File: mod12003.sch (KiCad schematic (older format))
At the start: 35 parts, among them J1 IN, J2 OUT, J3 IN, J4 OUT+, J5 OUT-, J8 DEVEL, Q1 AO4805, Q2 12A

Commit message: Remove OSHW logo
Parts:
- removed SYM1: OSHW-SCHEM-PCB6mm, mech:OSHW-6mm, symbol OSHW-SCHEM-PCB6mm
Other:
- note added: "Open hardware\nCPOHL 1.0 or greater"
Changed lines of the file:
@@
 Text Notes 700  6500 0    50   ~ 0
 Mating connector: A30980-ND
-$Comp
-L OSHW-SCHEM-PCB6mm SYM1
-U 1 1 55DBE608
-P 7800 7200
-F 0 "SYM1" H 7935 7200 50  0000 L CNN
-F 1 "OSHW-SCHEM-PCB6mm" H 7800 7150 50  0001 C CNN
-F 2 "mech:OSHW-6mm" H 7850 7100 50  0001 C CNN
-F 3 "" H 7800 7200 50  0000 C CNN
-	1    7800 7200
-	1    0    0    -1
-$EndComp
 Text Notes 7950 4050 0    50   ~ 10
 MOUNTING/HEAT SINKING:
@@
 Text Label 1200 6850 2    50   ~ 0
 PAD_MP1
+Text Notes 7650 7350 0    50   ~ 0
+Open hardware\nCPOHL 1.0 or greater
 $EndSCHEMATC

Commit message: Finish PCB
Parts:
- removed C2: 22n, IPC7351-Nominal:CAPC1608X55, symbol C-0603
- removed C3: 100n, IPC7351-Nominal:CAPC1608X55, symbol C-0603
- removed R1, R2, R52, R53: 470k, IPC7351-Nominal:RESC1608X50, symbol R-0603
- removed R4: 348, IPC7351-Nominal:RESC1608X50, symbol R-0603
- added C2: 22n, IPC7351-Nominal:CAPC1005X55, symbol C-0402
- added C3: 100n, IPC7351-Nominal:CAPC1005X55, symbol C-0402
- added R1, R2, R52, R53: 470k, IPC7351-Nominal:RESC1005X40, symbol R-0402
- added R4: 348, IPC7351-Nominal:RESC1005X40, symbol R-0402
- C58: value 1k/1kV -> 1n/1kV
- J3: value IN -> 24V
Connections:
- net GND: now also R1.1, R53.1
- net Linear/SCR_FIRE: now also C3.1, R4.2
- net OUT-: now also C3.2, R4.1
- net PAD_MP1: now also R52.2
- net V+: now also C2.1
- net VRP: now also R2.2
- net at C1.2, Q1.2 (G2), Q1.4 (G1): now also C2.2, R1.2, R2.1
- new net: R52.1, R53.2
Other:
- note added: "Additional parts:\nJ1, J2 mating connector: A30980-ND\nElastomer: 1168-1700-ND\nHeatsink insulator: 926-1489-ND"

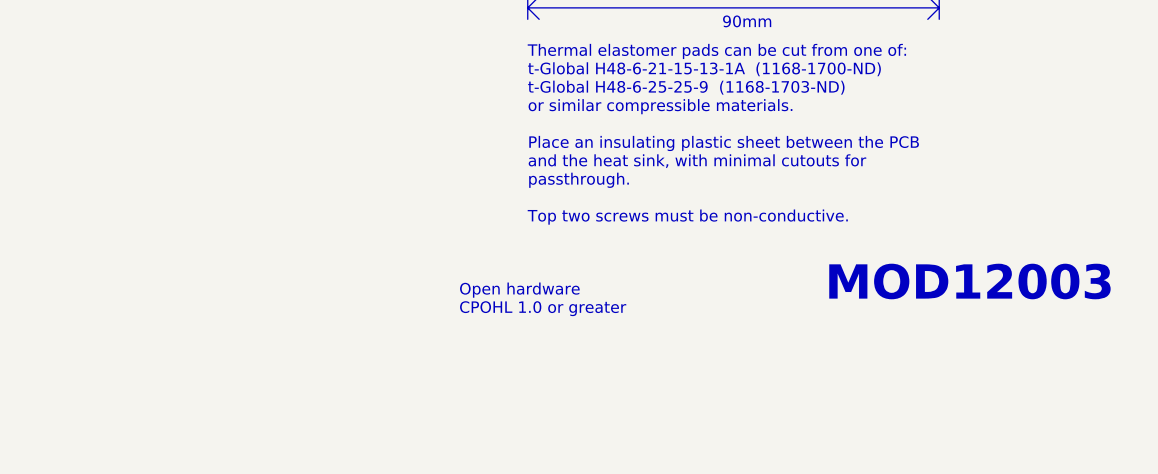
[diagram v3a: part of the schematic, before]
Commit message: Remove branding from schematic (may re-add later)
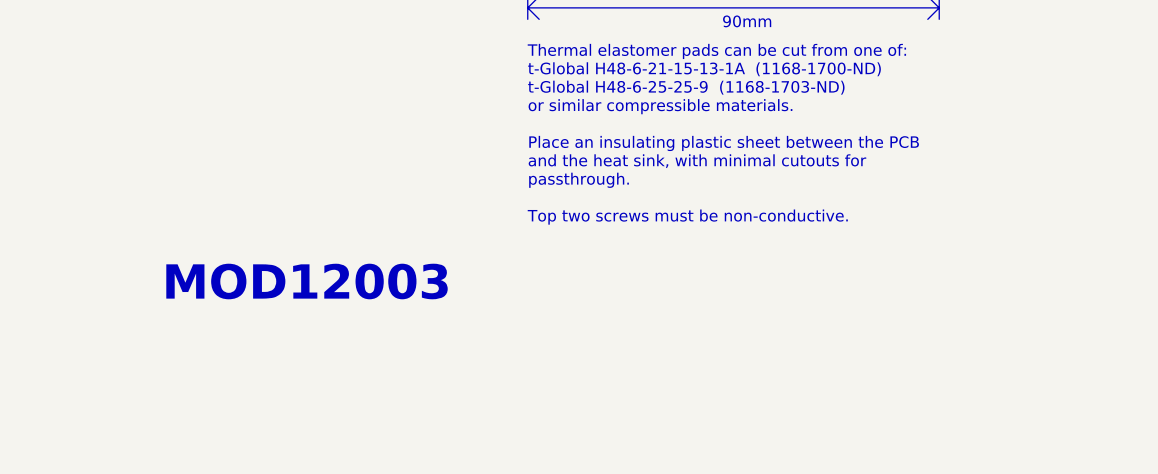
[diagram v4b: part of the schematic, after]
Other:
- note removed: "Open hardware\nCPOHL 1.0 or greater"
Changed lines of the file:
@@
 Text Notes 700  6350 0    50   ~ 0
 LOOP INTERFACE\n\nThe mainboard and all modules must be joined in a loop,\noutput of one connected to the input of the next. The sequence\nwill determine the logical ordering of the modules as seen\nby the user interface.
-Text Notes 9250 7300 0    150  ~ 30
+Text Notes 6350 7300 0    150  ~ 30
 MOD12003
 $Comp
@@
 Text Label 1200 6850 2    50   ~ 0
 PAD_MP1
-Text Notes 7650 7350 0    50   ~ 0
-Open hardware\nCPOHL 1.0 or greater
 Wire Wire Line
 	6600 4500 6600 4550

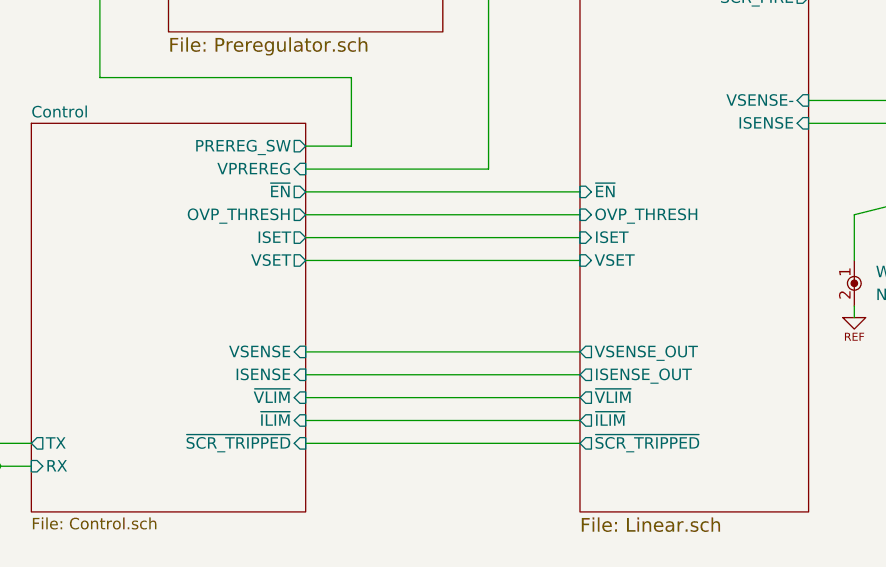
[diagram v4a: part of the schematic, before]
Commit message: Fix output blip
Add a bodge wire to prototype to allow the MCU to force the regulator
into saturation-low
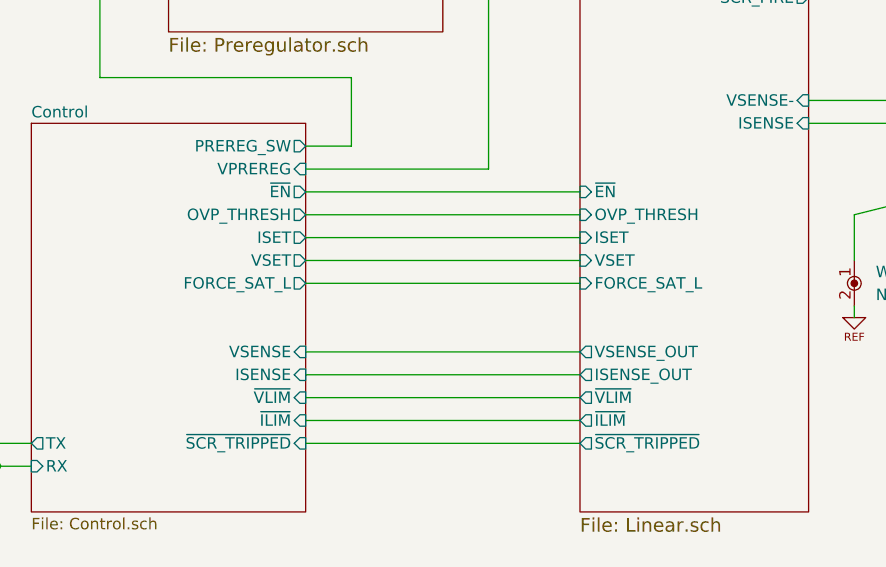
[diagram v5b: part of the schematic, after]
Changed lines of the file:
@@
 F15 "~ILIM" O L 5400 5000 50
 F16 "~SCR_TRIPPED" O L 5400 5100 50
+F17 "FORCE_SAT_L" I L 5400 4400 50
 $EndSheet
 $Comp
@@
 F13 "~SCR_TRIPPED" I R 4200 5100 50
 F14 "~EN" O R 4200 4000 50
+F15 "FORCE_SAT_L" O R 4200 4400 50
 $EndSheet
 $Comp
@@
 Text Notes 3150 6750 0    50   ~ 0
 Additional parts:\nJ1, J2 mating connector: A30980-ND\nElastomer: 1168-1700-ND\nHeatsink insulator: 926-1489-ND
+Wire Wire Line
+	4200 4400 5400 4400
 $EndSCHEMATC

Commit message: Update branding
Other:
- note removed: "MOD12003"
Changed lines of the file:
@@
 Sheet 1 6
 Title "20V, 3A hybrid power supply module"
-Date "2015-08-18"
-Rev ""
-Comp ""
-Comment1 ""
+Date "2015-11-17"
+Rev "preB"
+Comp "SEMIANALOG"
+Comment1 "MOD12003"
 Comment2 ""
-Comment3 ""
-Comment4 ""
+Comment3 "CC0: https://creativecommons.org/publicdomain/zero/1.0/"
+Comment4 "Source: https://github.com/semianalog/mod12003"
 $EndDescr
 $Sheet
@@
 Text Notes 700  6350 0    50   ~ 0
 LOOP INTERFACE\n\nThe mainboard and all modules must be joined in a loop,\noutput of one connected to the input of the next. The sequence\nwill determine the logical ordering of the modules as seen\nby the user interface.
-Text Notes 6350 7300 0    150  ~ 30
-MOD12003
 $Comp
 L +3.6 #PWR06

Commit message: Revise schematic
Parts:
- MP2, MP3: Value2 NYLON -> (none)
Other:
- note added: "Thermal elastomer pads can be cut from one of:\nt-Global H48-6-21-15-13-1A (1168-1700-ND)\nt-Global H48-6-25-25-9 (1168-1703-ND)\nor similar compressible materials."
- note removed: "METAL\nSCREW"
- note removed: "Thermal elastomer pads can be cut from one of:\nt-Global H48-6-21-15-13-1A (1168-1700-ND)\nt-Global H48-6-25-25-9 (1168-1703-ND)\nor similar compressible materials.\n\nPlace an insulating plastic sheet between the PCB\nand the heat sink, with minimal cutouts for\npassthrough.\n\nTop two screws must be non-conductive."
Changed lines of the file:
@@
 U 1 1 55CD1961
 P 750 7650
-F 0 "MP2" H 880 7720 50  0000 L CNN
-F 1 "SCREW" H 880 7620 50  0000 L CNN
+F 0 "MP2" H 880 7670 50  0000 L CNN
+F 1 "SCREW" H 880 7570 50  0000 L CNN
 F 2 "mech:SCREW-4-SUPPORTED" H 750 7650 50  0001 C CNN
 F 3 "" H 750 7650 60  0000 C CNN
-F 4 "NYLON" H 880 7520 50  0000 L CNN "Value2"
 	1    750  7650
 	1    0    0    -1
@@
 Text Notes 900  2250 0    50   ~ 0
 24V
-Text Notes 700  6350 0    50   ~ 0
+Text Notes 700  6150 0    50   ~ 0
 LOOP INTERFACE\n\nThe mainboard and all modules must be joined in a loop,\noutput of one connected to the input of the next. The sequence\nwill determine the logical ordering of the modules as seen\nby the user interface.
 $Comp
@@
 	1    0    0    1
 $EndComp
-Text Notes 700  6500 0    50   ~ 0
+Text Notes 700  6300 0    50   ~ 0
 Mating connector: A30980-ND
 Text Notes 7950 4050 0    50   ~ 10
@@
 Text Notes 9550 4250 0    30   ~ 0
 SCREW
-Text Notes 9350 5630 0    30   ~ 0
-METAL\nSCREW
 Text Notes 8900 4925 0    30   ~ 0
 THERMAL ELASTOMER
 Text Notes 8450 5475 0    30   ~ 0
 THERMAL ELASTOMER
-Text Notes 7950 6950 0    50   ~ 0
-Thermal elastomer pads can be cut from one of:\nt-Global H48-6-21-15-13-1A  (1168-1700-ND)\nt-Global H48-6-25-25-9  (1168-1703-ND)\nor similar compressible materials.\n\nPlace an insulating plastic sheet between the PCB\nand the heat sink, with minimal cutouts for\npassthrough.\n\nTop two screws must be non-conductive.
+Text Notes 7950 6400 0    50   ~ 0
+Thermal elastomer pads can be cut from one of:\nt-Global H48-6-21-15-13-1A  (1168-1700-ND)\nt-Global H48-6-25-25-9  (1168-1703-ND)\nor similar compressible materials.
 Wire Wire Line
 	10000 2400 9950 2500
@@
 F 2 "mech:SCREW-4-SUPPORTED" H 1250 7650 50  0001 C CNN
 F 3 "" H 1250 7650 60  0000 C CNN
-F 4 "NYLON" H 1380 7520 50  0000 L CNN "Value2"
 	1    1250 7650
 	1    0    0    -1
@@
 Wire Wire Line
 	4200 4400 5400 4400
+Text Notes 9350 5600 0    30   ~ 0
+SCREW
 $EndSCHEMATC
